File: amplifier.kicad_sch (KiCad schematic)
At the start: 8 parts, among them U1 TPA3118D2

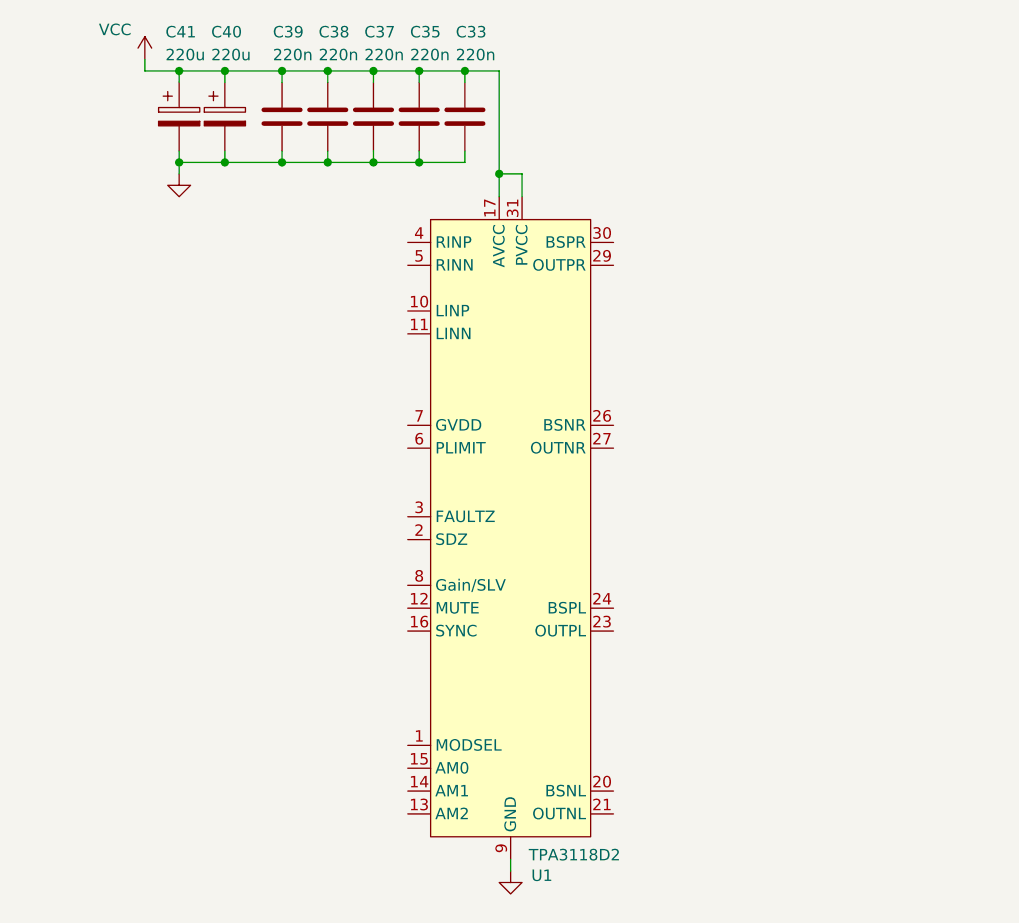
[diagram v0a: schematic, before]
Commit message: schem: add TPA3118 config components
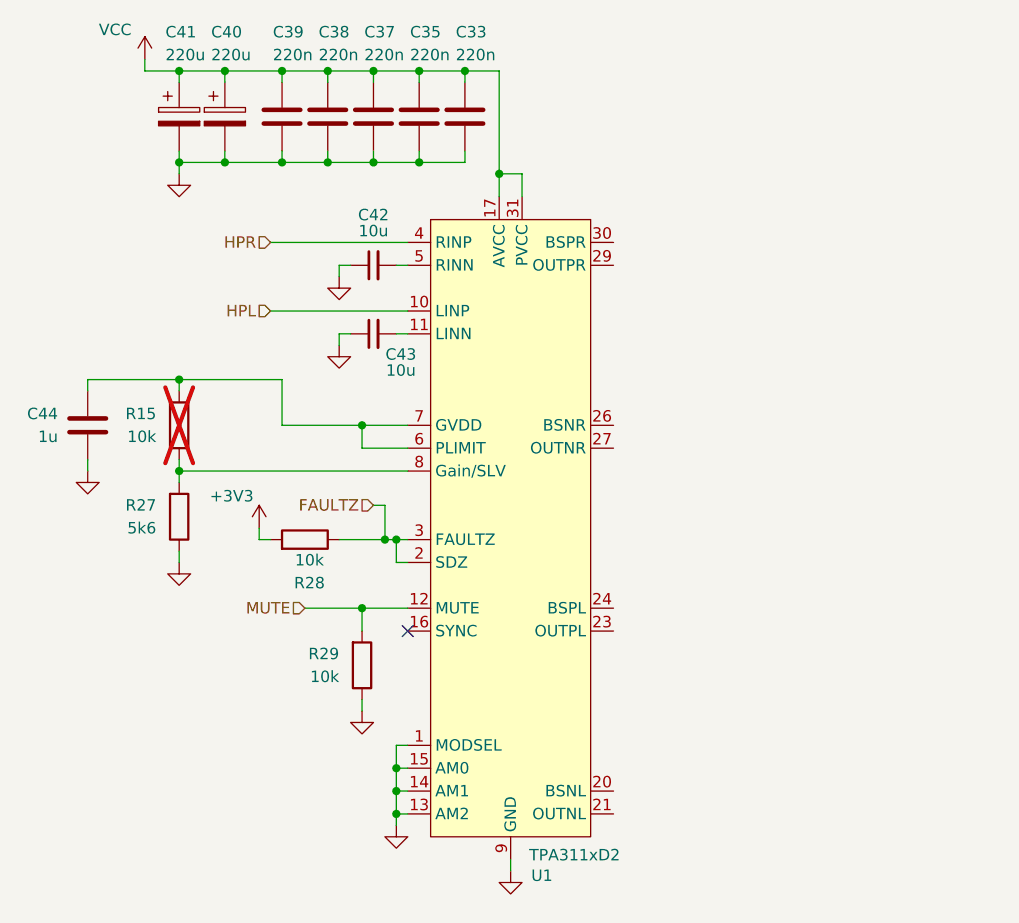
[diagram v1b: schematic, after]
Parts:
- added C42, C43: 10u, Capacitor_SMD:C_0805_2012Metric, symbol Device:C_Small
- added C44: 1u, Capacitor_SMD:C_0402_1005Metric, symbol Device:C
- added R15: 10k, Resistor_SMD:R_0603_1608Metric, symbol Device:R
- added R27: 5k6, Resistor_SMD:R_0603_1608Metric, symbol Device:R
- added R28, R29: 10k, Resistor_SMD:R_0402_1005Metric, symbol Device:R
- U1: value TPA3118D2 -> TPA311xD2
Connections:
- net GND: now also U1.1 (MODSEL), U1.13 (AM2), U1.14 (AM1), U1.15 (AM0), C42.1, C43.1, C44.2, R27.1, R29.1
- net HPL: now reaches U1.10 (LINP)
- net at U1.11 (LINN): now also C43.2
- net MUTE: now reaches U1.12 (MUTE)
- net MUTE: now also R29.2
- net FAULTZ: now reaches U1.2 (SDZ)
- net FAULTZ: now also U1.3 (FAULTZ), R28.1
- net HPR: now reaches U1.4 (RINP)
- net at U1.5 (RINN): now also C42.2
- net at U1.6 (PLIMIT): now also U1.7 (GVDD), C44.1, R15.2
- net at U1.8 (Gain/SLV): now also R15.1, R27.2
- new net +3V3: R28.2
- no-connect marks 0 -> 1

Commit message: schem: finish tpa3118 amplifier page
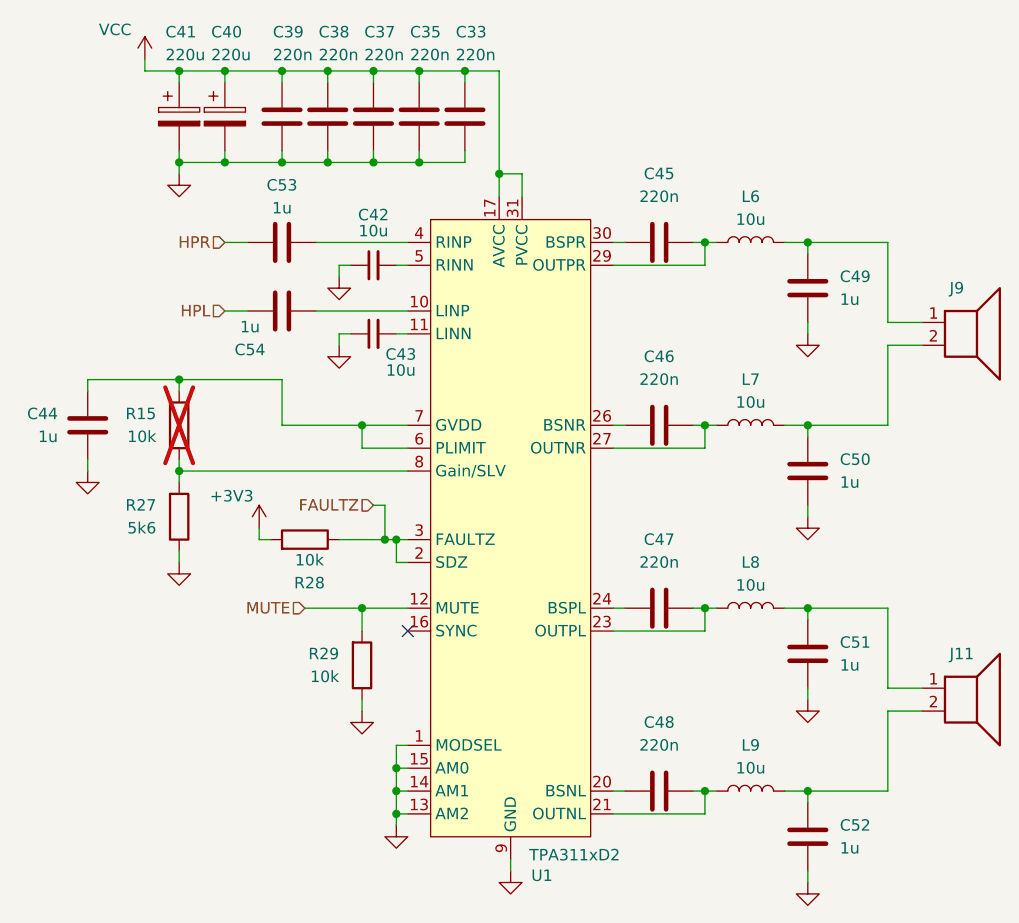
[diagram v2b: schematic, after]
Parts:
- added C45, C46, C47, C48: 220n, Capacitor_SMD:C_0402_1005Metric, symbol Device:C
- added C49, C50, C51, C52, C53, C54: 1u, Capacitor_SMD:C_0402_1005Metric, symbol Device:C
- added J11, J9: Conn_01x02, Connector_JST:JST_XH_B2B-XH-A_1x02_P2.50mm_Vertical, symbol Device:Speaker
- added L6, L7, L8, L9: 10u, Inductor_SMD:L_Vishay_IHLP-4040, symbol Device:L
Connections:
- net GND: now also C49.2, C50.2, C51.2, C52.2
- net HPL: now also C54.2; no longer U1.10 (LINP)
- net HPR: now also C53.1; no longer U1.4 (RINP)
- net at U1.20 (BSNL): now also C48.1
- net at U1.21 (OUTNL): now also C48.2, L9.1
- net at U1.23 (OUTPL): now also C47.2, L8.1
- net at U1.24 (BSPL): now also C47.1
- net at U1.26 (BSNR): now also C46.1
- net at U1.27 (OUTNR): now also C46.2, L7.1
- net at U1.29 (OUTPR): now also C45.2, L6.1
- net at U1.30 (BSPR): now also C45.1
- new net: C49.1, J9.1, L6.2
- new net: C50.1, J9.2, L7.2
- new net: C53.2, U1.4 (RINP)
- new net: C54.1, U1.10 (LINP)
- new net: C51.1, J11.1, L8.2
- new net: C52.1, J11.2, L9.2

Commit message: schem: add test points
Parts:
- added TP5: TestPoint, GLCS:TestPoint_Keystone_5015_Micro_Mini, symbol Connector:TestPoint
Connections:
- net PVCC: now also TP5.1
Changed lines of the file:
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@@
 	)
 	(junction
+		(at 146.05 49.53)
+		(diameter 0)
+		(color 0 0 0 0)
+	)
+	(junction
 		(at 110.49 85.09)
 		(diameter 0)
@@
 	(wire
 		(pts
-			(xy 146.05 52.07) (xy 146.05 40.64)
+			(xy 146.05 52.07) (xy 146.05 49.53)
 		)
 		(stroke
@@
 	(wire
 		(pts
+			(xy 146.05 49.53) (xy 146.05 40.64)
+		)
+		(stroke
+			(width 0)
+			(type default)
+		)
+	)
+	(wire
+		(pts
 			(xy 133.35 92.71) (xy 134.62 92.71)
 		)
@@
 					(unit 1)
 				)
+			)
+		)
+	)
+	(symbol
+		(lib_id "Connector:TestPoint")
+		(at 146.05 49.53 270)
+		(unit 1)
+		(body_style 1)
+		(exclude_from_sim no)
+		(in_bom yes)
+		(on_board yes)
+		(in_pos_files yes)
+		(dnp no)
+		(property "Reference" "TP5"
+			(at 151.384 47.752 0)
+			(show_name no)
+			(do_not_autoplace no)
+			(effects
+				(font
+					(size 1.27 1.27)
+				)
+				(justify left)
+			)
+		)
+		(property "Value" "TestPoint"
+			(at 148.0821 52.07 0)
+			(hide yes)
+			(show_name no)
+			(do_not_autoplace no)
+			(effects
+				(font
+					(size 1.27 1.27)
+				)
+				(justify left)
+			)
+		)
+		(property "Footprint" "GLCS:TestPoint_Keystone_5015_Micro_Mini"
+			(at 146.05 54.61 0)
+			(hide yes)
+			(show_name no)
+			(do_not_autoplace no)
+			(effects
+				(font
+					(size 1.27 1.27)
+				)
+			)
+		)
+		(property "Datasheet" ""
+			(at 146.05 54.61 0)
+			(hide yes)
+			(show_name no)
+			(do_not_autoplace no)
+			(effects
+				(font
+					(size 1.27 1.27)
+				)
+			)
+		)
+		(property "Description" "test point"
+			(at 146.05 49.53 0)
+			(hide yes)
+			(show_name no)
+			(do_not_autoplace no)
+			(effects
+				(font
+					(size 1.27 1.27)
+				)
+			)
+		)
+		(property "Basic" "X"
+			(at 146.05 49.53 0)
+			(hide yes)
+			(show_name no)
+			(do_not_autoplace no)
+			(effects
+				(font
+					(size 1.27 1.27)
+				)
+			)
+		)
+		(property "JLCPCB Part #" "C2906768"
+			(at 146.05 49.53 0)
+			(hide yes)
+			(show_name no)
+			(do_not_autoplace no)
+			(effects
+				(font
+					(size 1.27 1.27)
+				)
+			)
+		)
+		(property "Manufacturer" "Keystone"
+			(at 146.05 49.53 0)
+			(hide yes)
+			(show_name no)
+			(do_not_autoplace no)
+			(effects
+				(font
+					(size 1.27 1.27)
+				)
+			)
+		)
+		(property "Manufacturer Part Number" "5015"
+			(at 146.05 49.53 0)
+			(hide yes)
+			(show_name no)
+			(do_not_autoplace no)
+			(effects
+				(font
+					(size 1.27 1.27)
+				)
+			)
+		)
+		(pin "1"
+		)
+		(instances
+			(project "s6tm-stereo-dev-1"
+				(path "/41fad0d7-0cae-453e-a16c-bdf8be036e99/7a1ae675-5d8b-41bf-9106-c7cdfb2cabd6"
+					(reference "TP5")
+					(unit 1)
+				)

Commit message: schem: add missing footprints
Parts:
- U1: value TPA311xD2 -> TPA3118D2; footprint (none) -> Package_SO:HTSSOP-32-1EP_6.1x11mm_P0.65mm_EP5.2x11mm_Mask4.11x4.36mm_ThermalVias
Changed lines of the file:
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@@
 			)
 		)
-		(property "Value" "TPA311xD2"
+		(property "Value" "TPA3118D2"
 			(at 154.432 127.762 0)
 			(show_name no)
@@
 			)
 		)
-		(property "Footprint" ""
+		(property "Footprint" "Package_SO:HTSSOP-32-1EP_6.1x11mm_P0.65mm_EP5.2x11mm_Mask4.11x4.36mm_ThermalVias"
 			(at 148.59 92.71 0)
 			(hide yes)

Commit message: schem: add ordering info to BOM
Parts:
- C42, C43: JLCPCB Part # C16780 -> C440198; Manufacturer Samsung Electro-Mechanics -> Murata; Manufacturer Part Number CL21A476MQYNNNE -> GRM21BR61H106KE43L
- U1: Basic (none) -> X; JLCPCB Part # (none) -> C46497; Manufacturer (none) -> Texas Instruments; Manufacturer Part Number (none) -> TPA3118D2DAPR
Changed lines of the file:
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@@
 			)
 		)
-		(property "Manufacturer" "Samsung Electro-Mechanics "
+		(property "Manufacturer" "Murata"
 			(at 132.08 69.85 0)
 			(hide yes)
@@
 			)
 		)
-		(property "Manufacturer Part Number" "CL21A476MQYNNNE"
+		(property "Manufacturer Part Number" "GRM21BR61H106KE43L"
 			(at 132.08 69.85 0)
 			(hide yes)
@@
 			)
 		)
-		(property "JLCPCB Part #" "C16780"
+		(property "JLCPCB Part #" "C440198"
 			(at 132.08 69.85 0)
 			(hide yes)
@@
 		)
 		(property "Description" "30-W stereo, 60-W mono, 4.5- to 26-V supply, analog input Class-D audio amplifier"
+			(at 148.59 92.71 0)
+			(hide yes)
+			(show_name no)
+			(do_not_autoplace no)
+			(effects
+				(font
+					(size 1.27 1.27)
+				)
+			)
+		)
+		(property "Basic" "X"
+			(at 148.59 92.71 0)
+			(hide yes)
+			(show_name no)
+			(do_not_autoplace no)
+			(effects
+				(font
+					(size 1.27 1.27)
+				)
+			)
+		)
+		(property "JLCPCB Part #" "C46497"
+			(at 148.59 92.71 0)
+			(hide yes)
+			(show_name no)
+			(do_not_autoplace no)
+			(effects
+				(font
+					(size 1.27 1.27)
+				)
+			)
+		)
+		(property "Manufacturer" "Texas Instruments"
+			(at 148.59 92.71 0)
+			(hide yes)
+			(show_name no)
+			(do_not_autoplace no)
+			(effects
+				(font
+					(size 1.27 1.27)
+				)
+			)
+		)
+		(property "Manufacturer Part Number" "TPA3118D2DAPR"
 			(at 148.59 92.71 0)
 			(hide yes)
@@
 			)
 		)
-		(property "Manufacturer" "Samsung Electro-Mechanics "
+		(property "Manufacturer" "Murata"
 			(at 132.08 62.23 0)
 			(hide yes)
@@
 			)
 		)
-		(property "Manufacturer Part Number" "CL21A476MQYNNNE"
+		(property "Manufacturer Part Number" "GRM21BR61H106KE43L"
 			(at 132.08 62.23 0)
 			(hide yes)
@@
 			)
 		)
-		(property "JLCPCB Part #" "C16780"
+		(property "JLCPCB Part #" "C440198"
 			(at 132.08 62.23 0)
 			(hide yes)

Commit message: schem: add title
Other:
- company: (none) -> Rémi Ait-Younes
- title: (none) -> S6TM Stereo Dev 1
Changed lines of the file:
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@@
 	(generator_version "10.0")
 	(paper "A4")
+	(title_block
+		(title "S6TM Stereo Dev 1")
+		(date "2026-04-11")
+		(rev "01")
+		(company "Rémi Ait-Younes")
+	)
 	(junction
 		(at 110.49 50.8)

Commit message: schem: reannotate
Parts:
- renumbered C44 to C24, C41 to C25, C40 to C26, C39 to C27, C53 to C28, C54 to C29, C38 to C30, C37 to C31, C42 to C32, C43 to C33, C35 to C34, C33 to C35, C45 to C36, C46 to C37, C47 to C38, C48 to C39, C49 to C40, C50 to C41, C51 to C42, C52 to C43, J9 to J6, J11 to J7, R15 to R32, R27 to R33, R28 to R34, R29 to R35, TP5 to TP13, U1 to U4

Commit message: pcb: add audio layout
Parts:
- C32, C33: value 10u -> 1u; footprint Capacitor_SMD:C_0805_2012Metric -> Capacitor_SMD:C_0402_1005Metric; JLCPCB Part # C440198 -> C52923; Manufacturer Murata -> Samsung Electro-Mechanics; Manufacturer Part Number GRM21BR61H106KE43L -> CL05A105KA5NQNC
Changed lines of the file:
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@@
 	)
 	(symbol
+		(lib_id "Device:C_Small")
+		(at 132.08 69.85 90)
+		(unit 1)
+		(body_style 1)
+		(exclude_from_sim no)
+		(in_bom yes)
+		(on_board yes)
+		(in_pos_files yes)
+		(dnp no)
+		(property "Reference" "C33"
+			(at 126.492 68.834 90)
+			(show_name no)
+			(do_not_autoplace no)
+			(effects
+				(font
+					(size 1.27 1.27)
+				)
+			)
+		)
+		(property "Value" "1u"
+			(at 125.984 70.612 90)
+			(show_name no)
+			(do_not_autoplace no)
+			(effects
+				(font
+					(size 1.27 1.27)
+				)
+			)
+		)
+		(property "Footprint" "Capacitor_SMD:C_0402_1005Metric"
+			(at 132.08 69.85 0)
+			(hide yes)
+			(show_name no)
+			(do_not_autoplace no)
+			(effects
+				(font
+					(size 1.27 1.27)
+				)
+			)
+		)
+		(property "Datasheet" ""
+			(at 132.08 69.85 0)
+			(hide yes)
+			(show_name no)
+			(do_not_autoplace no)
+			(effects
+				(font
+					(size 1.27 1.27)
+				)
+			)
+		)
+		(property "Description" "Unpolarized capacitor, small symbol"
+			(at 132.08 69.85 0)
+			(hide yes)
+			(show_name no)
+			(do_not_autoplace no)
+			(effects
+				(font
+					(size 1.27 1.27)
+				)
+			)
+		)
+		(property "Manufacturer" "Samsung Electro-Mechanics "
+			(at 132.08 69.85 0)
+			(hide yes)
+			(show_name no)
+			(do_not_autoplace no)
+			(effects
+				(font
+					(size 1.27 1.27)
+				)
+			)
+		)
+		(property "Manufacturer Part Number" "CL05A105KA5NQNC"
+			(at 132.08 69.85 0)
+			(hide yes)
+			(show_name no)
+			(do_not_autoplace no)
+			(effects
+				(font
+					(size 1.27 1.27)
+				)
+			)
+		)
+		(property "Basic" "Y"
+			(at 132.08 69.85 0)
+			(hide yes)
+			(show_name no)
+			(do_not_autoplace no)
+			(effects
+				(font
+					(size 1.27 1.27)
+				)
+			)
+		)
+		(property "JLCPCB Part #" "C52923"
+			(at 132.08 69.85 0)
+			(hide yes)
+			(show_name no)
+			(do_not_autoplace no)
+			(effects
+				(font
+					(size 1.27 1.27)
+				)
+			)
+		)
+		(pin "1"
+		)
+		(pin "2"
+		)
+		(instances
+			(project "s6tm-stereo-dev-1"
+				(path "/41fad0d7-0cae-453e-a16c-bdf8be036e99/7a1ae675-5d8b-41bf-9106-c7cdfb2cabd6"
+					(reference "C33")
+					(unit 1)
+				)
+			)
+		)
+	)
+	(symbol
 		(lib_id "power:GND")
 		(at 180.34 110.49 0)
@@
 	)
 	(symbol
-		(lib_id "Device:C_Small")
-		(at 132.08 69.85 90)
+		(lib_id "Device:C")
+		(at 163.83 80.01 90)
 		(unit 1)
 		(body_style 1)
@@
 		(in_pos_files yes)
 		(dnp no)
-		(property "Reference" "C33"
-			(at 135.128 72.136 90)
+		(fields_autoplaced yes)
+		(property "Reference" "C37"
+			(at 163.83 72.39 90)
 			(show_name no)
 			(do_not_autoplace no)
@@
 			)
 		)
-		(property "Value" "10u"
-			(at 135.128 73.914 90)
+		(property "Value" "220n"
+			(at 163.83 74.93 90)
 			(show_name no)
 			(do_not_autoplace no)
@@
 			)
 		)
-		(property "Footprint" "Capacitor_SMD:C_0805_2012Metric"
-			(at 132.08 69.85 0)
+		(property "Footprint" "Capacitor_SMD:C_0402_1005Metric"
+			(at 167.64 79.0448 0)
 			(hide yes)
 			(show_name no)
@@
 		)
 		(property "Datasheet" ""
-			(at 132.08 69.85 0)
+			(at 163.83 80.01 0)
 			(hide yes)
 			(show_name no)
@@
 			)
 		)
-		(property "Description" "Unpolarized capacitor, small symbol"
-			(at 132.08 69.85 0)
+		(property "Description" "Unpolarized capacitor"
+			(at 163.83 80.01 0)
 			(hide yes)
 			(show_name no)
@@
 			)
 		)
-		(property "Manufacturer" "Murata"
-			(at 132.08 69.85 0)
+		(property "Manufacturer" "Samsung Electro-Mechanics "
+			(at 163.83 80.01 0)
 			(hide yes)
 			(show_name no)
@@
 			)
 		)
-		(property "Manufacturer Part Number" "GRM21BR61H106KE43L"
-			(at 132.08 69.85 0)
+		(property "Manufacturer Part Number" "CL05B224KO5NNNC"
+			(at 163.83 80.01 0)
 			(hide yes)
 			(show_name no)
@@
 		)
 		(property "Basic" "Y"
-			(at 132.08 69.85 0)
+			(at 163.83 80.01 0)
 			(hide yes)
 			(show_name no)
@@
 			)
 		)
-		(property "JLCPCB Part #" "C440198"
-			(at 132.08 69.85 0)
+		(property "JLCPCB Part #" "C16772"
+			(at 163.83 80.01 0)
 			(hide yes)
 			(show_name no)
@@
 			(project "s6tm-stereo-dev-1"
 				(path "/41fad0d7-0cae-453e-a16c-bdf8be036e99/7a1ae675-5d8b-41bf-9106-c7cdfb2cabd6"
-					(reference "C33")
+					(reference "C37")
 					(unit 1)
 				)
@@
 	)
 	(symbol
-		(lib_id "Device:C")
-		(at 163.83 80.01 90)
+		(lib_id "Device:C_Small")
+		(at 132.08 62.23 90)
 		(unit 1)
 		(body_style 1)
@@
 		(in_pos_files yes)
 		(dnp no)
-		(fields_autoplaced yes)
-		(property "Reference" "C37"
-			(at 163.83 72.39 90)
+		(property "Reference" "C32"
+			(at 126.492 61.214 90)
 			(show_name no)
 			(do_not_autoplace no)
@@
 			)
 		)
-		(property "Value" "220n"
-			(at 163.83 74.93 90)
+		(property "Value" "1u"
+			(at 125.984 62.992 90)
 			(show_name no)
 			(do_not_autoplace no)
@@
 		)
 		(property "Footprint" "Capacitor_SMD:C_0402_1005Metric"
-			(at 167.64 79.0448 0)
+			(at 132.08 62.23 0)
 			(hide yes)
 			(show_name no)
@@
 		)
 		(property "Datasheet" ""
-			(at 163.83 80.01 0)
+			(at 132.08 62.23 0)
 			(hide yes)
 			(show_name no)
@@
 			)
 		)
-		(property "Description" "Unpolarized capacitor"
-			(at 163.83 80.01 0)
+		(property "Description" "Unpolarized capacitor, small symbol"
+			(at 132.08 62.23 0)
 			(hide yes)
 			(show_name no)
@@
 		)
 		(property "Manufacturer" "Samsung Electro-Mechanics "
-			(at 163.83 80.01 0)
+			(at 132.08 62.23 0)
 			(hide yes)
 			(show_name no)
@@
 			)
 		)
-		(property "Manufacturer Part Number" "CL05B224KO5NNNC"
-			(at 163.83 80.01 0)
+		(property "Manufacturer Part Number" "CL05A105KA5NQNC"
+			(at 132.08 62.23 0)
 			(hide yes)
 			(show_name no)
@@
 		)
 		(property "Basic" "Y"
-			(at 163.83 80.01 0)
+			(at 132.08 62.23 0)
 			(hide yes)
 			(show_name no)
@@
 			)
 		)
-		(property "JLCPCB Part #" "C16772"
-			(at 163.83 80.01 0)
+		(property "JLCPCB Part #" "C52923"
+			(at 132.08 62.23 0)
 			(hide yes)
 			(show_name no)
@@
 			(project "s6tm-stereo-dev-1"
 				(path "/41fad0d7-0cae-453e-a16c-bdf8be036e99/7a1ae675-5d8b-41bf-9106-c7cdfb2cabd6"
-					(reference "C37")
+					(reference "C32")
 					(unit 1)
 				)
@@
 					(unit 1)
 				)
-			)
-		)
-	)
-	(symbol
-		(lib_id "Device:C_Small")
-		(at 132.08 62.23 90)
-		(unit 1)
-		(body_style 1)
-		(exclude_from_sim no)
-		(in_bom yes)
-		(on_board yes)
-		(in_pos_files yes)
-		(dnp no)
-		(property "Reference" "C32"
-			(at 132.08 56.642 90)
-			(show_name no)
-			(do_not_autoplace no)
-			(effects
-				(font
-					(size 1.27 1.27)
-				)
-			)
-		)
-		(property "Value" "10u"
-			(at 132.08 58.42 90)
-			(show_name no)
-			(do_not_autoplace no)
-			(effects
-				(font
-					(size 1.27 1.27)
-				)
-			)
-		)
-		(property "Footprint" "Capacitor_SMD:C_0805_2012Metric"
-			(at 132.08 62.23 0)
-			(hide yes)
-			(show_name no)
-			(do_not_autoplace no)
-			(effects
-				(font
-					(size 1.27 1.27)
-				)
-			)
-		)
-		(property "Datasheet" ""
-			(at 132.08 62.23 0)
-			(hide yes)
-			(show_name no)
-			(do_not_autoplace no)
-			(effects
-				(font
-					(size 1.27 1.27)
-				)
-			)
-		)
-		(property "Description" "Unpolarized capacitor, small symbol"
-			(at 132.08 62.23 0)
-			(hide yes)
-			(show_name no)
-			(do_not_autoplace no)
-			(effects
-				(font
-					(size 1.27 1.27)
-				)
-			)
-		)
-		(property "Manufacturer" "Murata"
-			(at 132.08 62.23 0)
-			(hide yes)
-			(show_name no)
-			(do_not_autoplace no)
-			(effects
-				(font
-					(size 1.27 1.27)
-				)
-			)
-		)
-		(property "Manufacturer Part Number" "GRM21BR61H106KE43L"
-			(at 132.08 62.23 0)
-			(hide yes)
-			(show_name no)
-			(do_not_autoplace no)
-			(effects
-				(font
-					(size 1.27 1.27)
-				)
-			)
-		)
-		(property "Basic" "Y"
-			(at 132.08 62.23 0)
-			(hide yes)
-			(show_name no)
-			(do_not_autoplace no)
-			(effects
-				(font
-					(size 1.27 1.27)
-				)
-			)
-		)
-		(property "JLCPCB Part #" "C440198"
-			(at 132.08 62.23 0)
-			(hide yes)
-			(show_name no)
-			(do_not_autoplace no)
-			(effects
-				(font
-					(size 1.27 1.27)
-				)
-			)
-		)
-		(pin "1"
-		)
-		(pin "2"
-		)
-		(instances
-			(project "s6tm-stereo-dev-1"
-				(path "/41fad0d7-0cae-453e-a16c-bdf8be036e99/7a1ae675-5d8b-41bf-9106-c7cdfb2cabd6"
-					(reference "C32")
-					(unit 1)
-				)
